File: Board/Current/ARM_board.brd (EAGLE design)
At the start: 101.6 x 81.3 mm, 155 parts, among them IC3 STM32F437VI, IC4 LM358DT, J1 USART/I2C, J10 ANALOG, J11 DGND, J12 DPWR, J13 DIGITAL, J14 SGND, J15 SPWR, J16 SERVO, J2 I2C2/USART3, J3 USART2, J5 SPI, J6 Bluesmirf, J7 SWD, J8 AGND, J9 APWR, Q1 STL4P2UH7, Q2 2STR1230, SW1 SW, U1 LSM330DLC, U10 BAV99, U11 BAV99, U12 USBLC6-2, U13 USBLC6-2, U14 STMPS2171MTR, U15 MC74HC164, U16 STL85N6F3, U2 RT7259, U3 NC7SZU04, U4 L6206Q, U5 L6206Q, U6 SI7617, U7 SI7617, U8 SI7617, U9 SI7617, Y2 8MHz

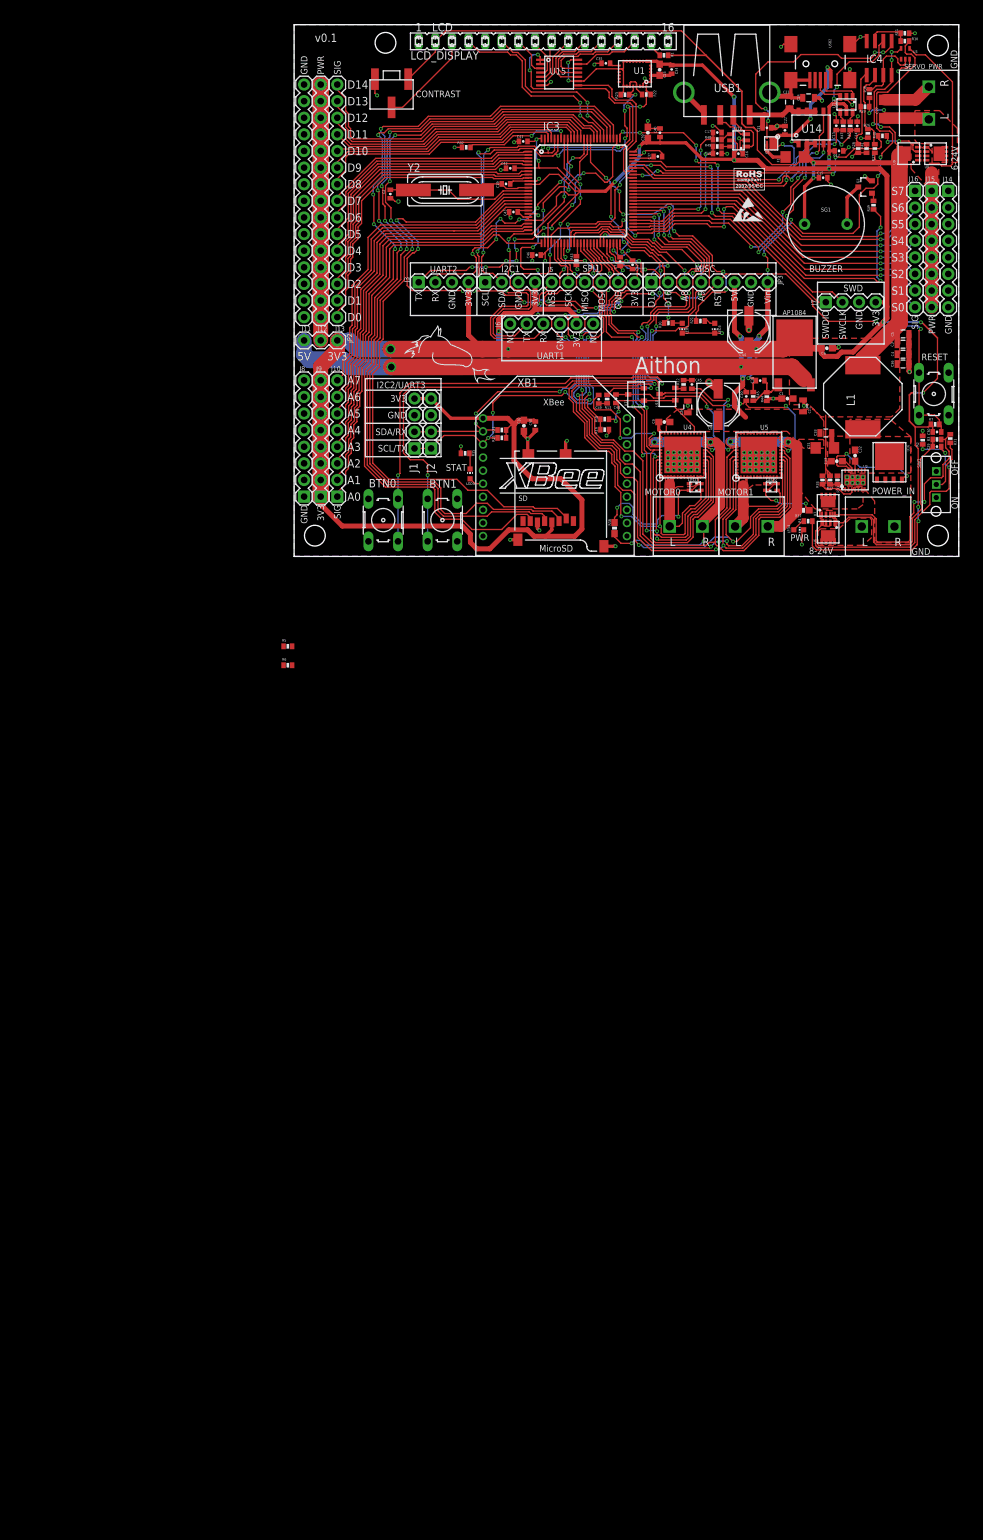
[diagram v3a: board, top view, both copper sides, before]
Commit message: Starting updating the schematic for the new switching regulator.
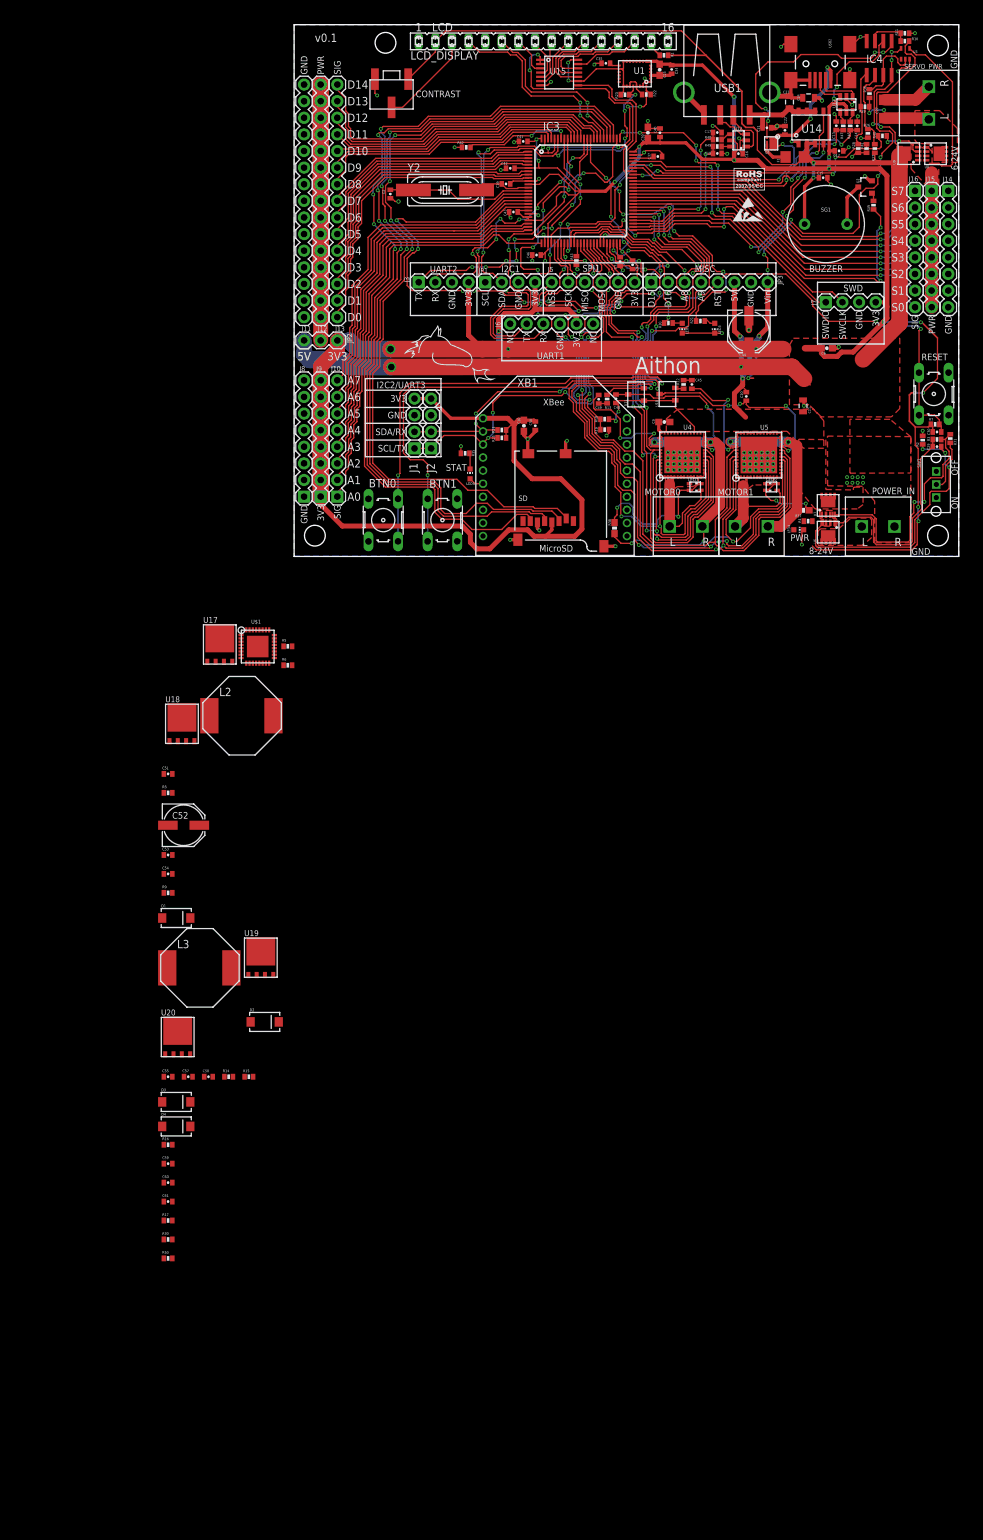
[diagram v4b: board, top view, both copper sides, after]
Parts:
- removed AP1084: AP1084, r_cubed:DPAK
- removed C1, C33: 10u, SparkFun:0603-CAP
- removed C26, C28: 10u, SparkFun:0805
- removed C3, C36, C4, C5: 22u, SparkFun:0805
- removed C31: 22u, SparkFun:1206
- removed C32: 1u, SparkFun:0603-CAP
- removed C38: 0.1u, SparkFun:0402-CAP
- removed C8: 100u, SparkFun:PANASONIC_D
- removed L1: 2.7u, r_cubed:INDUCTOR
- removed R32: 93.1k, SparkFun:0402-RES
- removed R33: 18k, SparkFun:0402-RES
- removed R34: 100k, SparkFun:0402-RES
- removed R44: 2k, SparkFun:0402-RES
- removed R45: 1.21k, SparkFun:0402-RES
- removed U16: STL85N6F3, r_cubed:POWERFLAT5X6
- removed U2: RT7259, r_cubed:WDFN-14L
- added C51, C53, C54, C55, C57, C58, C59, C60, C61: ?, SparkFun:0402-CAP
- added C52: ?, SparkFun:PANASONIC_D
- added D1, D2, D3, D4: (no value), SparkFun:SMA-DIODE
- added L2, L3: ?, r_cubed:INDUCTOR
- added R14, R15, R16, R8, R9: ?, SparkFun:0402-RES
- added R17, R30, R50: 100k, SparkFun:0402-RES
- added U$1: PM6685, r_cubed:VFQFPN-32
- added U17, U18, U19, U20: ?, r_cubed:POWERFLAT5X6
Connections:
- removed net MPOWER: C11.1, C20.1, C26.1, C28.1, C31.1, C48.1, C8.+, C9.1, JP3.8, R10.2, R18.1, R34.2, U10.1, U11.1, U2.4, U2.5, U2.6, U4.26, U4.27, U4.34, U4.35, U5.26, U5.27, U5.34, U5.35, U7.5, U7.6, U7.7, U7.8, U7.PAD
- removed net N$10: C32.2, L1.P$1, U16.5, U2.10, U2.8, U2.9
- removed net N$17: R32.1, R33.2, U2.1
- removed net N$20: C33.2, U2.12
- removed net N$25: C32.1, U2.11
- removed net N$32: AP1084.1, C38.2, R44.2, R45.1
- removed net N$35: U16.4, U2.13
- removed net N$44: R34.1, U2.3
- new net N$55: R8.2, U$1.20
- new net N$56: U$1.22, U17.4
- new net N$57: U$1.15, U18.4
- new net N$59: C51.1, D3.C, U$1.23
- new net N$66: C51.2, D1.C, L2.P$1, R8.1, U$1.21, U17.1, U17.2, U17.3, U18.5
- new net N$67: C54.2, R9.1
- new net N$69: C53.1, C54.1, U$1.30
- new net N$72: U$1.13, U20.4
- new net N$73: U$1.10, U19.4
- new net N$74: C55.1, D4.C, U$1.9
- new net N$75: C55.2, D2.C, L3.P$1, R14.1, U$1.11, U19.1, U19.2, U19.3, U20.5
- new net N$76: R14.2, U$1.12
- new net N$77: C57.1, C58.1, U$1.2
- new net N$78: C58.2, R15.1
- new net N$79: C59.1, R16.2, U$1.19
- new net N$80: C60.1, U$1.32
- new net N$81: C61.1, U$1.18, U$1.3, U$1.31
- new net N$82: R30.2, U$1.5
- new net N$83: R17.2, U$1.4
- new net N$84: R50.2, U$1.25
- new net VIN: C11.1, C20.1, C48.1, C9.1, D3.A, D4.A, JP3.8, R10.2, R16.1, R17.1, R18.1, R30.1, R50.1, U10.1, U11.1, U17.5, U19.5, U4.26, U4.27, U4.34, U4.35, U5.26, U5.27, U5.34, U5.35, U7.5, U7.6, U7.7, U7.8, U7.PAD
- net +3V3: now also L3.P$2, R15.2, U$1.8; no longer AP1084.TAB, C38.1, R45.2
- net 5V: now also C52.+, L2.P$2, R9.2, U$1.29; no longer AP1084.3, C1.1, C3.1, C36.1, C4.1, C5.1, L1.P$2, R32.2
- net GND: now also C52.-, C53.2, C57.2, C59.2, C60.2, C61.2, D1.A, D2.A, U$1.1, U$1.14, U$1.16, U$1.17, U$1.24, U$1.28, U$1.PAD, U18.1, U18.2, U18.3, U20.1, U20.2, U20.3; no longer C1.2, C26.2, C28.2, C3.2, C31.2, C33.1, C36.2, C4.2, C5.2, C8.-, R33.1, R44.1, U16.1, U16.2, U16.3, U2.14, U2.P$1
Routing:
- net VIN: track 0.00 -> 105.5 mm, vias 0 -> 9
- net MPOWER: track 105.5 -> 0.00 mm, vias 9 -> 0
- net N$35: track 16.9 -> 0.00 mm, vias 2 -> 0
- net GND: track 141.8 -> 128.6 mm, vias 109 -> 105
- net +3V3: track 563.5 -> 551.0 mm
- net 5V: track 283.1 -> 270.9 mm
- net N$32: track 6.77 -> 0.00 mm
- net N$44: track 5.77 -> 0.00 mm
- net N$17: track 2.67 -> 0.00 mm
- net N$20: track 2.27 -> 0.00 mm
- net N$9: track 2.15 -> 0.00 mm
- net N$25: track 1.43 -> 0.00 mm
- added copper zone on layer 1, net VIN
- removed copper zone on layer 1, net MPOWER

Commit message: Made more progress on switching regulator.
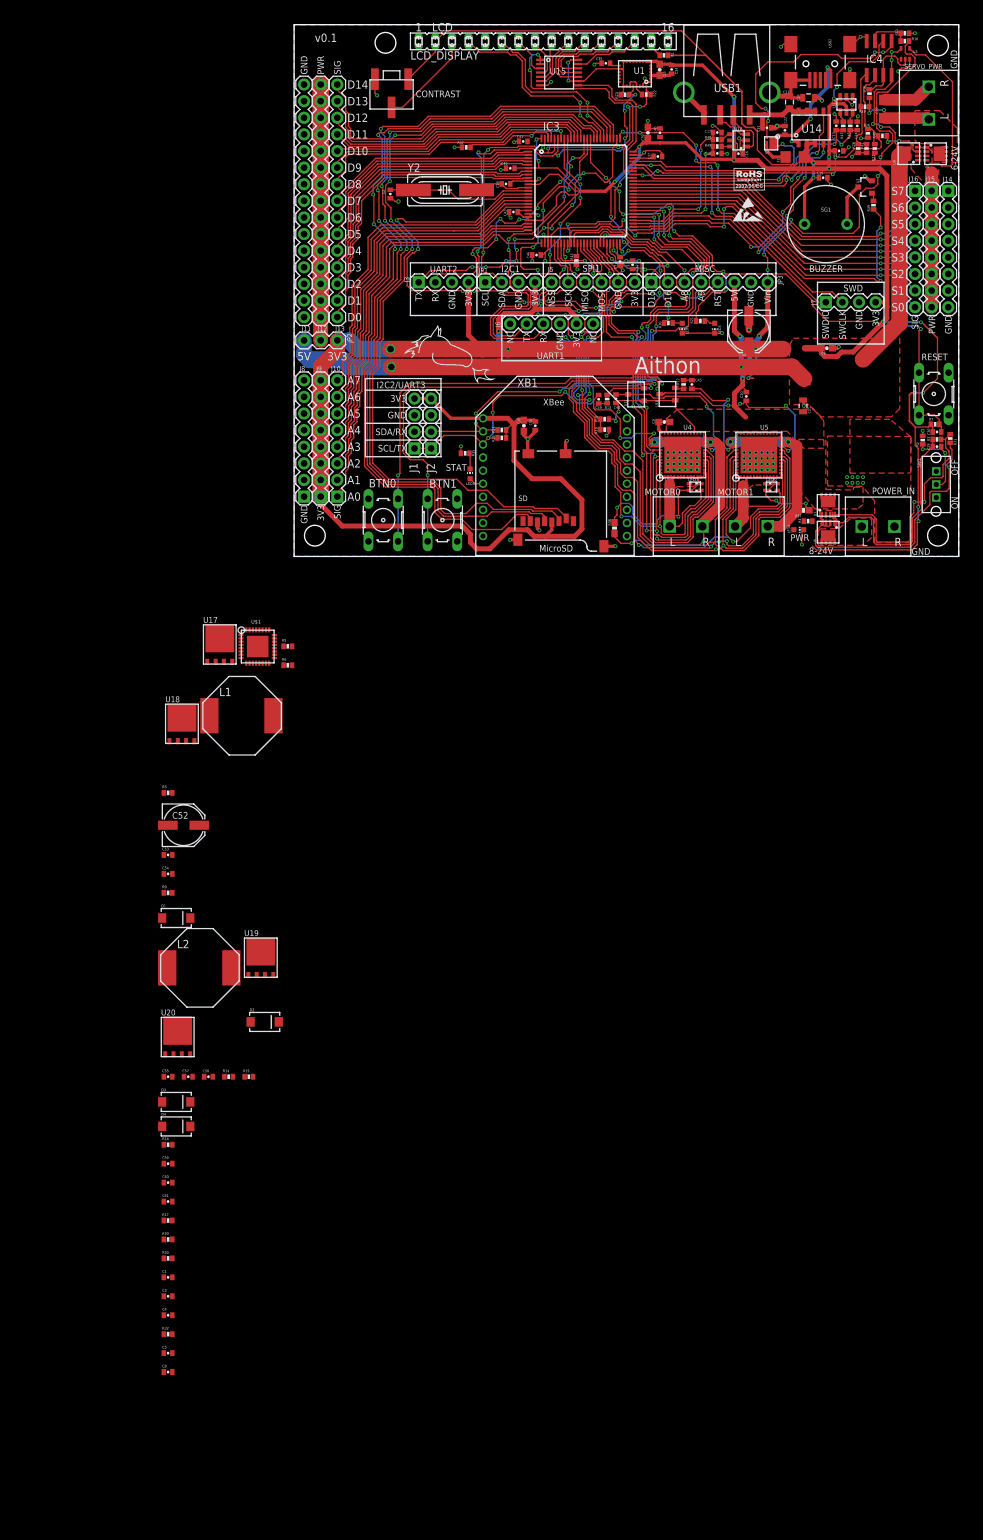
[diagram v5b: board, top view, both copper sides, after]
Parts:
- removed C51: ?, SparkFun:0402-CAP
- removed L3: ?, r_cubed:INDUCTOR
- added C1, C8: 0.1u, SparkFun:0402-CAP
- added C3, C4: 15u, SparkFun:0402-CAP
- added C5: 1u, SparkFun:0402-CAP
- added L1: 1.5uH, r_cubed:INDUCTOR
- added R32: 47, SparkFun:0402-RES
- C53, C57: value ? -> 47p
- C55, C60: value ? -> 0.1u
- C58: value ? -> 100p
- C59, C61: value ? -> 4.7u
- D1, D2: value (none) -> STPS1L30M
- L2: value ? -> 3.3uH
- R15: value ? -> 1k
- R16: value ? -> 3.9
- moved L2 39.1 mm to (-19.4, -62.9)
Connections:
- removed net N$59: C51.1, D3.C, U$1.23
- removed net N$81: C61.1, U$1.18, U$1.3, U$1.31
- new net LDO5: C61.1, R32.2, U$1.18, U$1.3
- new net N$20: C5.1, R32.1, U$1.31
- new net N$25: C8.1, D3.C, U$1.23
- net +3V3: now also L2.P$2; no longer L3.P$2
- net 5V: now also L1.P$2; no longer L2.P$2
- net GND: now also C1.2, C3.2, C4.2, C5.2
- net N$66: now also C8.2, L1.P$1; no longer C51.2, L2.P$1
- net N$75: now also L2.P$1; no longer L3.P$1
- net N$79: now also C1.1
- net VIN: now also C3.1, C4.1
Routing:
- net N$17: track 6.50 -> 0.00 mm
- net +3V3: track 551.0 -> 544.8 mm
- net N$8: track 5.02 -> 0.00 mm
- net USB_5V: track 58.0 -> 56.5 mm
- net GND: track 128.6 -> 127.9 mm

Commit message: Made changes to switching regulator section of schematic.
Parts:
- C54: value ? -> 100p
- R14: value ? -> 220
- R8: value ? -> 510
- R9: value ? -> 1k
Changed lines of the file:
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@@
 <element name="L1" library="r_cubed" package="INDUCTOR" value="1.5uH" x="-12.954" y="-24.35351875"/>
 <element name="U18" library="r_cubed" package="POWERFLAT5X6" value="?" x="-17.145" y="-25.587959375"/>
-<element name="R8" library="SparkFun" package="0402-RES" value="?" x="-19.263359375" y="-36.141659375"/>
+<element name="R8" library="SparkFun" package="0402-RES" value="510" x="-19.263359375" y="-36.141659375"/>
 <element name="C52" library="SparkFun" package="PANASONIC_D" value="?" x="-16.893540625" y="-41.094659375"/>
 <element name="C53" library="SparkFun" package="0402-CAP" value="47p" x="-19.263359375" y="-45.63618125"/>
-<element name="C54" library="SparkFun" package="0402-CAP" value="?" x="-19.263359375" y="-48.53178125"/>
-<element name="R9" library="SparkFun" package="0402-RES" value="?" x="-19.263359375" y="-51.42738125"/>
+<element name="C54" library="SparkFun" package="0402-CAP" value="100p" x="-19.263359375" y="-48.53178125"/>
+<element name="R9" library="SparkFun" package="0402-RES" value="1k" x="-19.263359375" y="-51.42738125"/>
 <element name="D1" library="SparkFun" package="SMA-DIODE" value="STPS1L30M" x="-18.01368125" y="-55.27548125"/>
 <element name="U19" library="r_cubed" package="POWERFLAT5X6" value="?" x="-5.090159375" y="-61.33338125"/>
@@
 <element name="U20" library="r_cubed" package="POWERFLAT5X6" value="?" x="-17.80031875" y="-73.46441875"/>
 <element name="C55" library="SparkFun" package="0402-CAP" value="0.1u" x="-19.263359375" y="-79.537559375"/>
-<element name="R14" library="SparkFun" package="0402-RES" value="?" x="-10.005059375" y="-79.537559375"/>
+<element name="R14" library="SparkFun" package="0402-RES" value="220" x="-10.005059375" y="-79.537559375"/>
 <element name="C57" library="SparkFun" package="0402-CAP" value="47p" x="-16.177259375" y="-79.537559375"/>
 <element name="C58" library="SparkFun" package="0402-CAP" value="100p" x="-13.091159375" y="-79.537559375"/>
@@
 </signal>
 <signal name="N$74">
-<contactref element="C55" pad="1"/>
 <contactref element="U$1" pad="9"/>
 <contactref element="D4" pad="C"/>
+<contactref element="C55" pad="1"/>
 <wire x1="-19.913359375" y1="-79.537559375" x2="-15.86368125" y2="-87.1347" width="0" layer="19" extent="1-1"/>
 <wire x1="-7.3126" y1="-16.326959375" x2="-19.913359375" y2="-79.537559375" width="0" layer="19" extent="1-1"/>

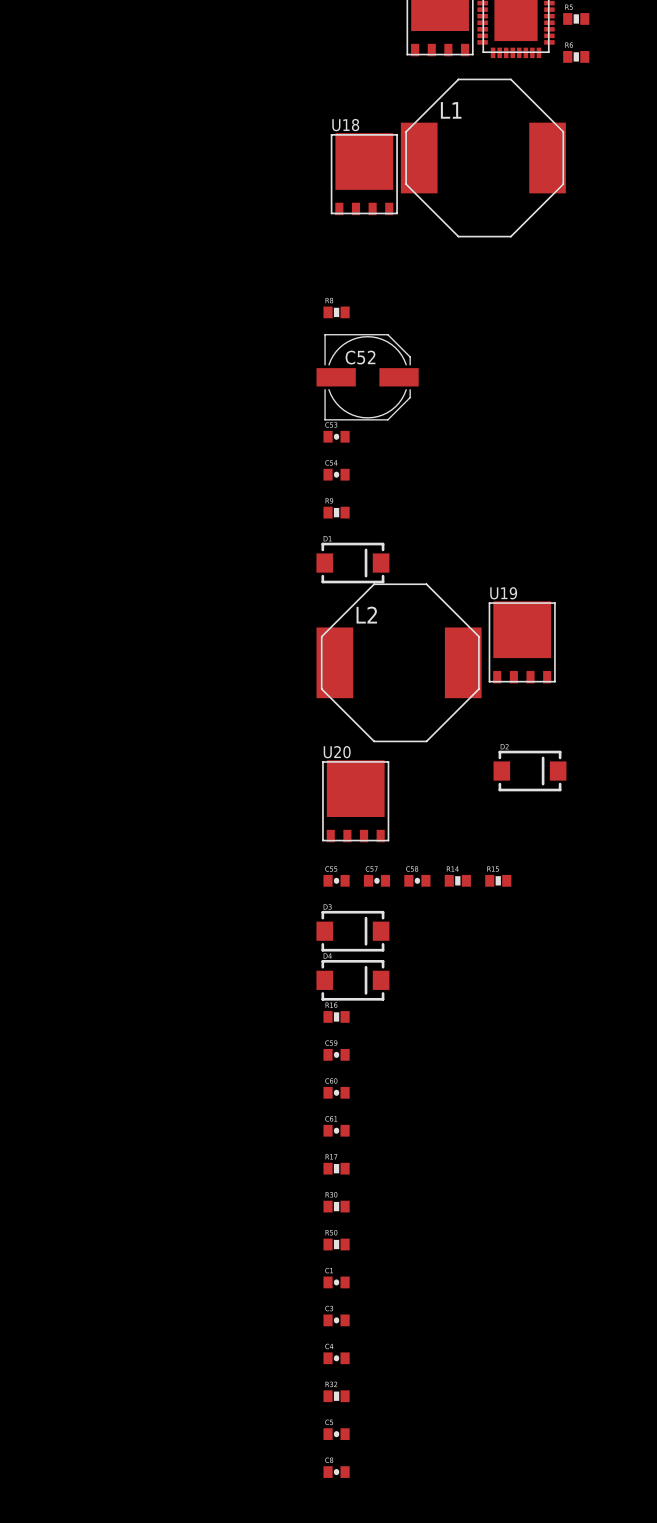
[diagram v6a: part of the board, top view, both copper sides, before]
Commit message: Created parts for Issue 44
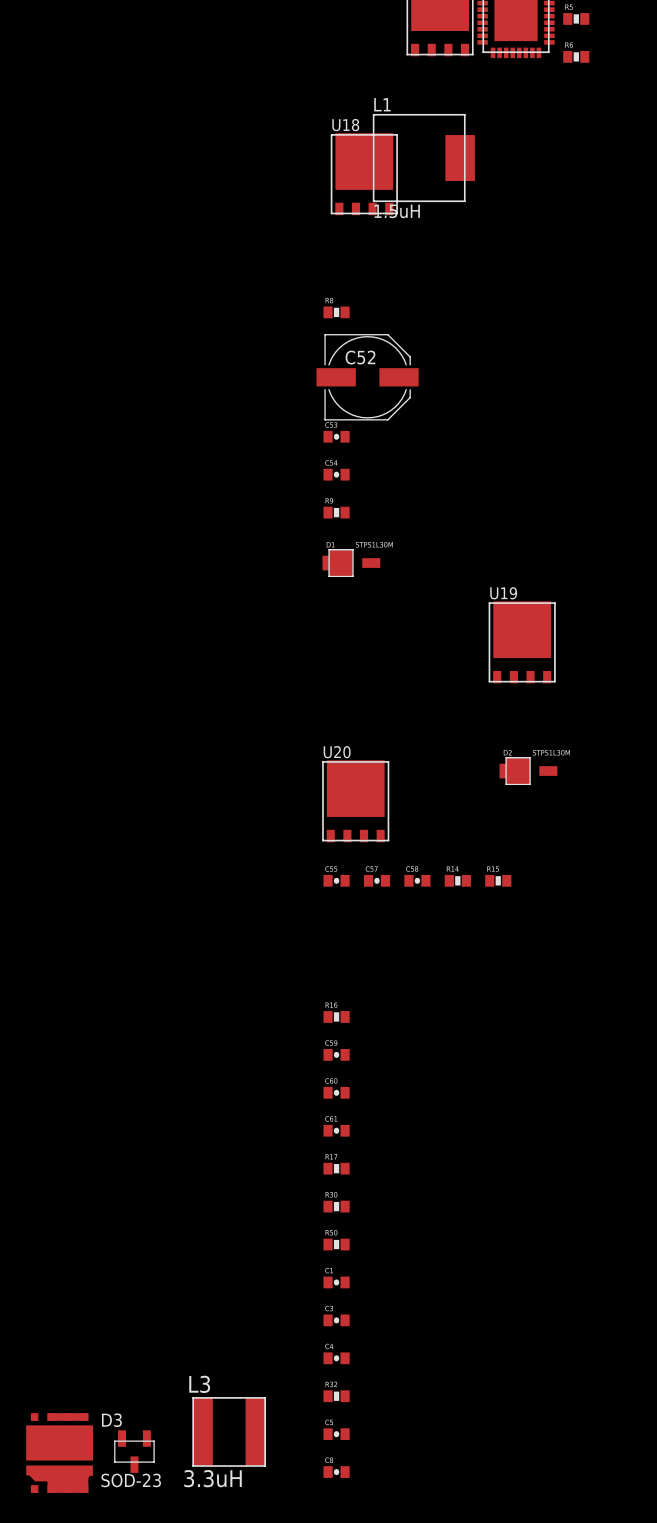
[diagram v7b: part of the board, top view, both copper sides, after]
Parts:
- removed D4: (no value), SparkFun:SMA-DIODE
- removed L2: 3.3uH, r_cubed:INDUCTOR
- added L3: 3.3uH, r_cubed:INDUCTOR-0520CDMCDS
- added U$2: DUAL-MOSFET, r_cubed:DUAL-MOSFET-STL60N32N3LL
- D1, D2: device SparkFun:SMA-DIODE -> SparkFun:STPS1L30M
- D3: value (none) -> SOD-23; device SparkFun:SMA-DIODE -> r_cubed:SOT-23
- L1: device r_cubed:INDUCTOR -> r_cubed:INDUCTOR-LMIP707
- moved D3 43.1 mm to (-34.7, -123.1)
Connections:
- net +3V3: now also L3.P$2; no longer L2.P$2
- net GND: now also D1.P$1, D2.P$1; no longer D1.A, D2.A
- net N$25: now also D3.P$1; no longer D3.C
- net N$66: now also D1.P$2; no longer D1.C
- net N$74: now also D3.P$2; no longer D4.C
- net N$75: now also D2.P$2, L3.P$1; no longer D2.C, L2.P$1
- net VIN: now also D3.P$0; no longer D3.A, D4.A
